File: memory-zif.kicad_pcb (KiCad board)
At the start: 2 copper layers, 101.6 x 44.5 mm, 10 parts, among them J1 Conn_01x30_Male, SW1 SW_DPDT_x2, U1 28C256, U2 74LS04, U3 HM62256BLP

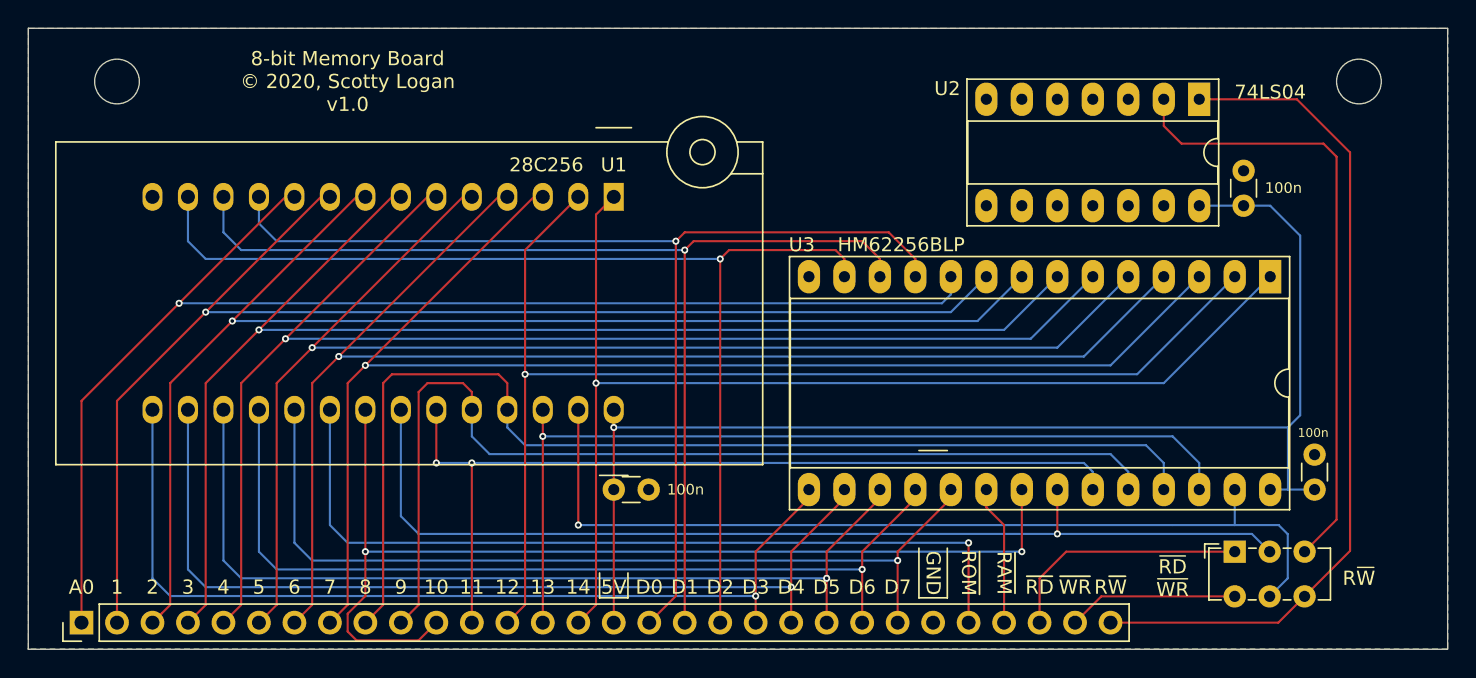
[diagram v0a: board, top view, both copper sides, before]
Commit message: using 128K RAM rather than 32K RAM
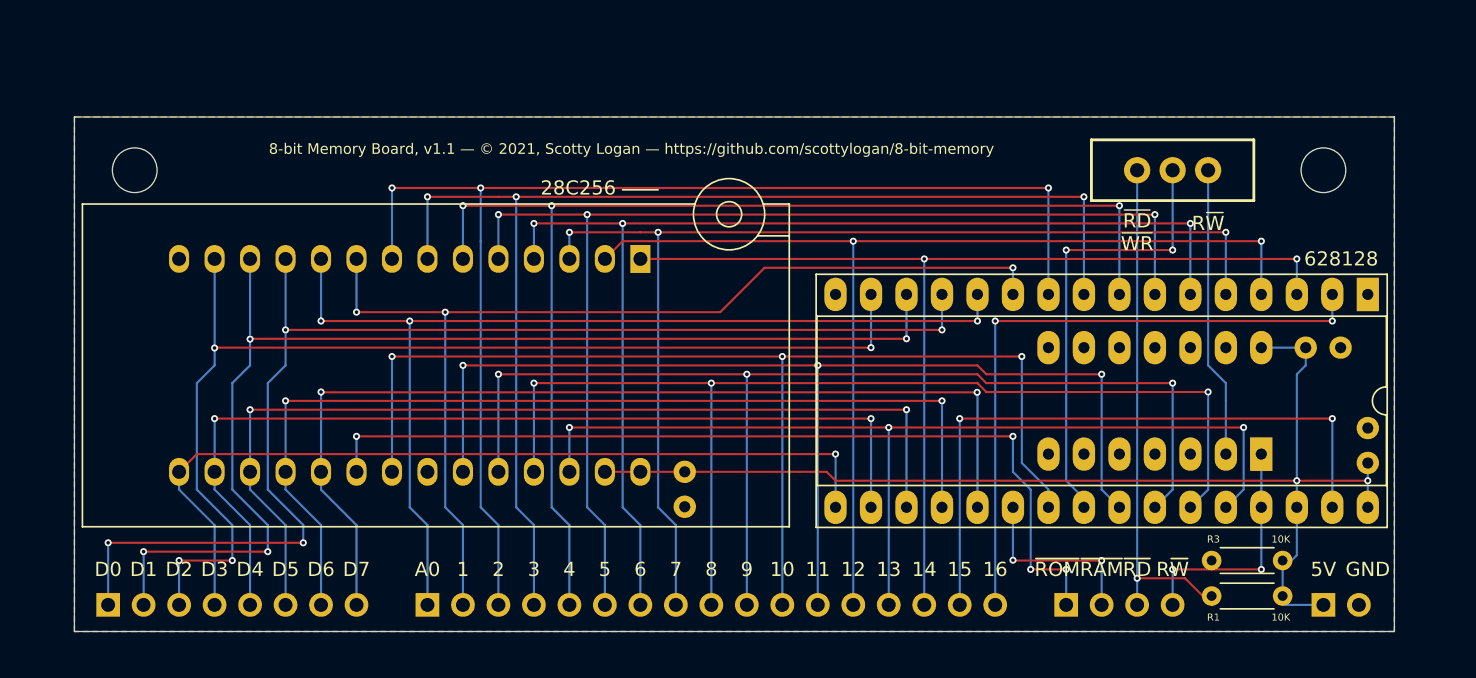
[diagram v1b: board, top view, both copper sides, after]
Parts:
- added J2: DATA, Connector_PinHeader_2.54mm:PinHeader_1x08_P2.54mm_Vertical, B.Cu at (107.3, 92.1)
- added J3: CONTROL, Connector_PinHeader_2.54mm:PinHeader_1x04_P2.54mm_Vertical, B.Cu at (175.9, 92.1)
- added J4: POWER, Connector_PinHeader_2.54mm:PinHeader_1x02_P2.54mm_Vertical, B.Cu at (194.3, 92.1)
- added R1: 10K, Resistor_THT:R_Axial_DIN0204_L3.6mm_D1.6mm_P5.08mm_Horizontal, F.Cu at (191.4, 91.4)
- added R3: 10K, Resistor_THT:R_Axial_DIN0204_L3.6mm_D1.6mm_P5.08mm_Horizontal, F.Cu at (191.4, 88.9)
- C1, C2, C3, U2: moved to B.Cu
- J1: value Conn_01x30_Male -> ADDRESS; footprint Connector_PinHeader_2.54mm:PinHeader_1x30_P2.54mm_Vertical -> Connector_PinHeader_2.54mm:PinHeader_1x17_P2.54mm_Vertical; moved to B.Cu
- SW1: value SW_DPDT_x2 -> SW_SPDT; footprint Button_Switch_THT:SW_E-Switch_EG1271_DPDT -> Switches:SWITCH_SPDT_PTH_11.6X4.0MM
- U3: value HM62256BLP -> 628128; footprint Package_DIP:DIP-28_W15.24mm_Socket_LongPads -> Package_DIP:DIP-32_W15.24mm_Socket_LongPads
- moved SW1 27.7 mm to (183.5, 61.0), turned to 90 degrees
- moved U2 25.8 mm to (189.9, 81.3), turned to 90 degrees
- moved J1 24.8 mm to (130.2, 92.1), turned to 270 degrees
- moved C2 11.1 mm to (193.0, 73.7), turned to 0 degrees
- moved U3 7.10 mm to (197.5, 69.8)
- moved H2 6.84 mm to (194.3, 61.0)
- moved H1 6.48 mm to (109.2, 61.0)
- moved C3 5.24 mm to (148.6, 82.5), turned to 270 degrees
- moved U1 4.84 mm to (145.4, 67.3)
- moved C1 4.26 mm to (197.5, 81.9)
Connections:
- J1 pad 16: +5V -> /A15
- J1 pad 17: /D0 -> /A16
- U1 pad 22: /~OE -> GND
- U1 pad 27: /~WE -> +5V
- U3 pad 1: /A14 -> Net-(U3-Pad1)
- U3 pad 10: /A0 -> /A2
- U3 pad 11: /D0 -> /A1
- U3 pad 12: /D1 -> /A0
- U3 pad 13: /D2 -> /D0
- U3 pad 14: GND -> /D1
- U3 pad 15: /D3 -> /D2
- U3 pad 16: /D4 -> GND
- U3 pad 17: /D5 -> /D3
- U3 pad 18: /D6 -> /D4
- U3 pad 19: /D7 -> /D5
- U3 pad 2: /A12 -> /A16
- U3 pad 20: /~RAM -> /D6
- U3 pad 21: /A10 -> /D7
- U3 pad 22: /~OE -> /~RAM
- U3 pad 23: /A11 -> /A10
- U3 pad 24: /A9 -> /~OE
- U3 pad 25: /A8 -> /A11
- U3 pad 26: /A13 -> /A9
- U3 pad 27: /~WE -> /A8
- U3 pad 28: +5V -> /A13
- U3 pad 3: /A7 -> /A14
- U3 pad 4: /A6 -> /A12
- U3 pad 5: /A5 -> /A7
- U3 pad 6: /A4 -> /A6
- U3 pad 7: /A3 -> /A5
- U3 pad 8: /A2 -> /A4
- U3 pad 9: /A1 -> /A3
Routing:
- net /~WE: track 66.8 -> 0.00 mm, vias 1 -> 0
- net /A16: track 0.00 -> 46.4 mm, vias 0 -> 2
- net /A15: track 0.00 -> 46.4 mm, vias 0 -> 2
- net /R~W: track 60.2 -> 17.8 mm, vias 0 -> 2
- net /~OE: track 74.0 -> 32.3 mm, vias 1 -> 2
- net /~R~W: track 44.4 -> 20.8 mm
- net /A0: track 93.9 -> 74.2 mm, vias 1 -> 3
- net /~RD: track 17.9 -> 37.2 mm, vias 0 -> 1
- net /A7: track 99.5 -> 80.5 mm, vias 1 -> 3
- net /A1: track 94.1 -> 76.1 mm, vias 1 -> 3
- net /A11: track 63.8 -> 80.8 mm, vias 2 -> 3
- net /A6: track 98.6 -> 82.4 mm, vias 1 -> 3
- net /A5: track 97.7 -> 84.3 mm, vias 1 -> 3
- net /~WR: track 12.2 -> 0.00 mm
- net /A4: track 96.8 -> 86.3 mm, vias 1 -> 3
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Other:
- board size 101.6 x 44.5 mm -> 94.5 x 36.8 mm
- board text added: "15"
- board text added: "16"
- board text added: "8-bit Memory Board, v1.1 — © 2021, Scotty Logan — https://github.com/scottylogan/8-bit-memory"
- board text removed: "8-bit Memory Board © 2020, Scotty Logan v1.0"
- board text removed: "8-bit Memory Board, v1.0 © 2020, Scotty Logan https://github.com/scottylogan/8-bit-memory"
- board text removed: "~WR"
